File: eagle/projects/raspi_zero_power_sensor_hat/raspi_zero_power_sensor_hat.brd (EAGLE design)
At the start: 65 x 30 mm, 158 parts, among them J301 MOL-SL-2-RA, J302 USB_MICROB_RECPT, J401 MOL-SL-2-RA, J402 MOL-SL-2-V, J601 RECEPTACLE-2x5-2.54MM, J602 MOL-SL-4-RA, J603 MOL-SL-3-V, J604 RECEPTACLE-2x3-2.54MM, Q301 SSM6N7002KFU, Q401 SSM6N7002KFU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

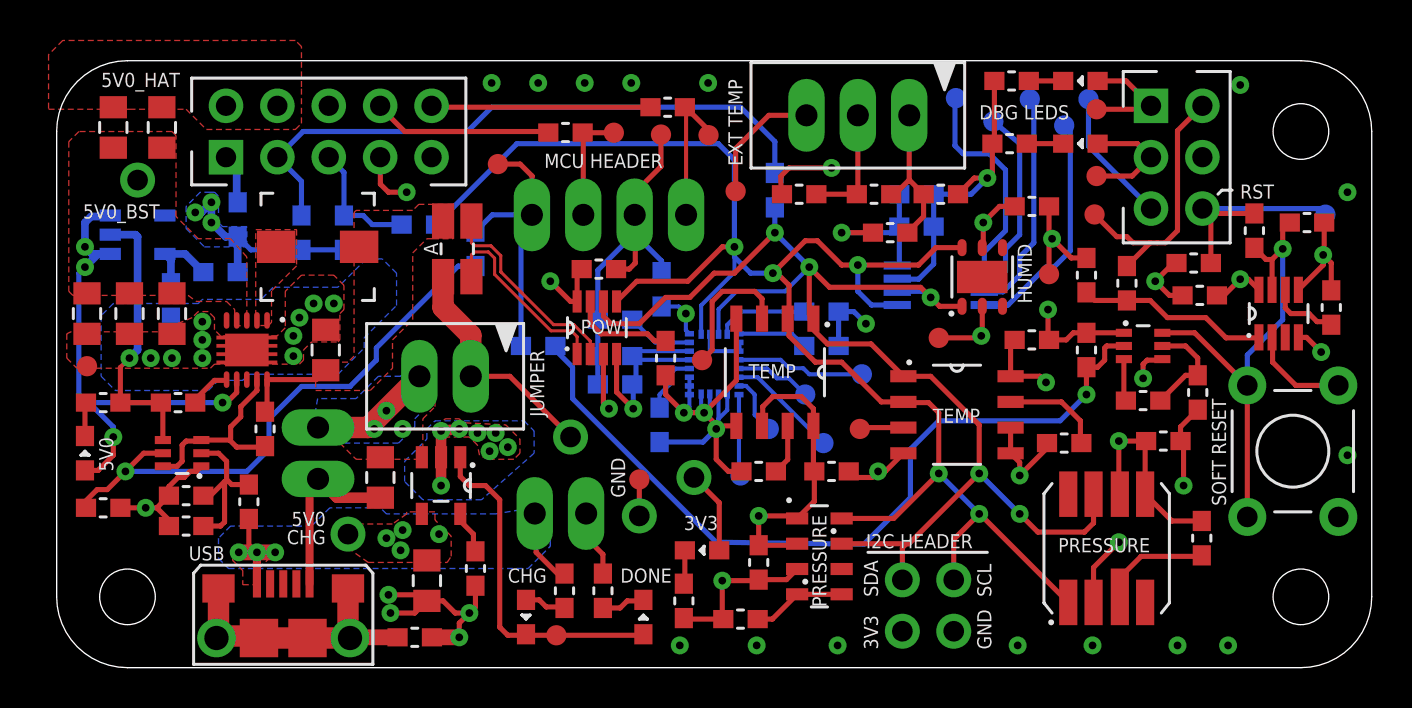
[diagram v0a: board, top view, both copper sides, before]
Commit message: modified TP pad widths. Moved Power monitor to allow for vertical SL population of the MCU header
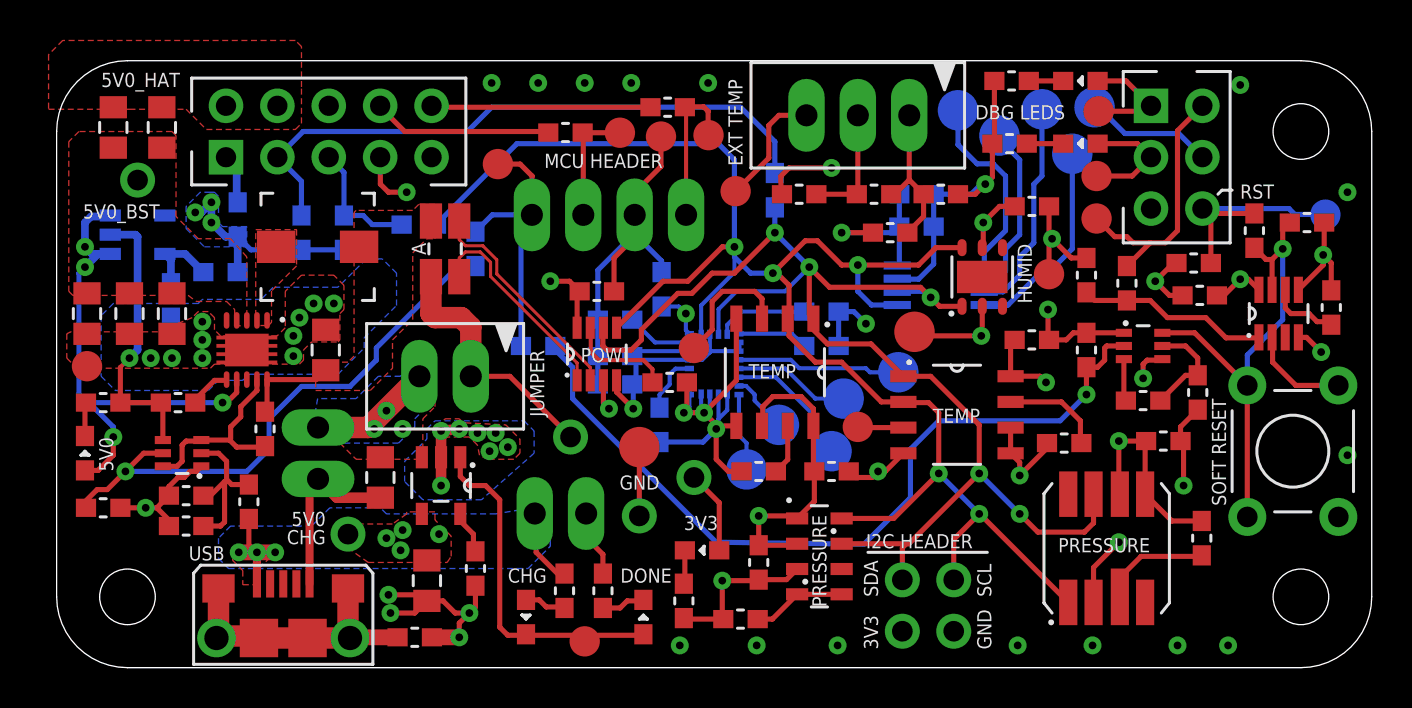
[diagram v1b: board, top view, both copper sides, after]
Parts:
- TP303, TP501, TP502, TP503, TP504, TP505, TP508, TP509, TP510, TP511, TP512, TP513: device daqcs:TP10R -> daqcs:TP20R
- TP304, TP404, TP506, TP507, TP605, TP606, TP607, TP608, TP609, TP610, TP611, TP612, TP613, TP614: device daqcs:TP10R -> daqcs:TP15R
- moved TP509 1.91 mm to (38.9, 13.3)
- moved TP508 1.80 mm to (41.6, 14.6)
- moved TP303 1.60 mm to (28.8, 10.9)
- moved TP501 1.46 mm to (50.2, 25.4)
- moved TP304 1.43 mm to (26.1, 1.30)
- moved U504 1.30 mm to (26.7, 15.5)
- moved TP513 1.24 mm to (42.4, 16.6)
- moved R504 1.22 mm to (30.3, 14.1), turned to 180 degrees
- moved C506 1.10 mm to (26.7, 18.6)
- moved TP502 0.78 mm to (48.7, 27.6)
- moved TP503 0.76 mm to (46.6, 26.3)
- moved TP507 0.72 mm to (31.5, 15.8)
- moved TP504 0.61 mm to (44.5, 27.6)
- moved R402 0.60 mm to (19.2, 20.7)
- moved TP510 0.57 mm to (38.3, 10.7)
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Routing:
- net IMU_INT_M: track 3.81 -> 5.79 mm
- net IMU_DRDY_M: track 6.37 -> 8.13 mm
- net ADC_AIN3_REF: track 11.7 -> 10.2 mm
- net PP3V3_HAT: track 86.4 -> 85.1 mm
- net IMU_INT1_AG: track 5.52 -> 6.62 mm
- net VBAT_J: track 11.7 -> 12.7 mm
- net I2C1_RASPI_SDA: track 65.9 -> 66.9 mm
- net ADC_AIN1: track 9.50 -> 8.61 mm
- net VBAT_SNS_N: track 10.2 -> 11.1 mm
- net VBAT_SNS_P: track 9.57 -> 10.4 mm
- net GND: track 177.7 -> 178.5 mm
- net UART_RASPI_RXD_MCU_TXD: track 7.25 -> 8.03 mm
- net I2C1_RASPI_SCL: track 83.7 -> 84.3 mm
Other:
- board text added: "X"
- board text added: "Y"
- board text added: "Z"

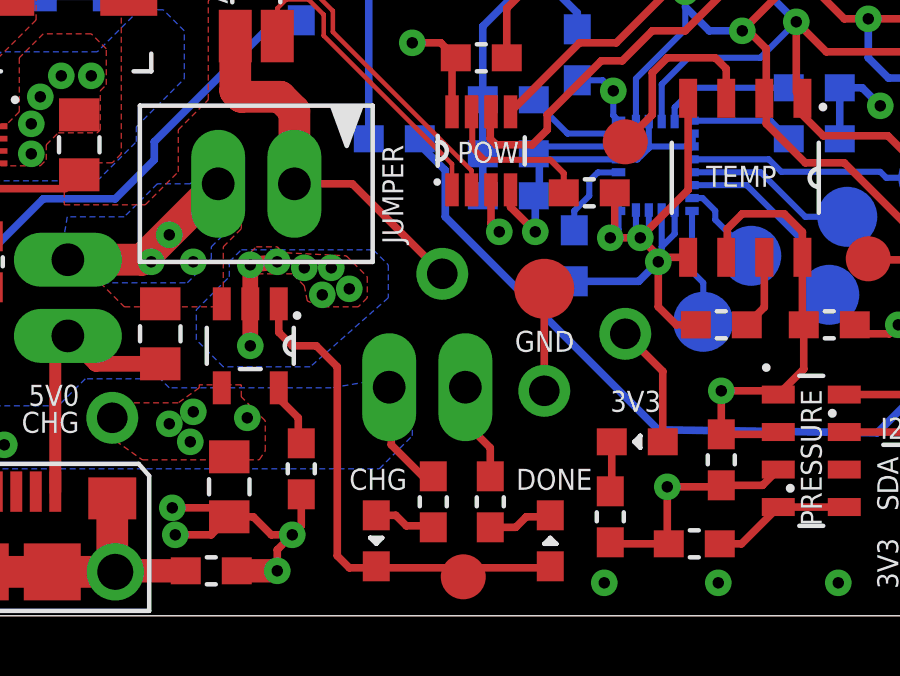
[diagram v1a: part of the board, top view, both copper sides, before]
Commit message: moved components around SL charge connector so a vertical one can be used
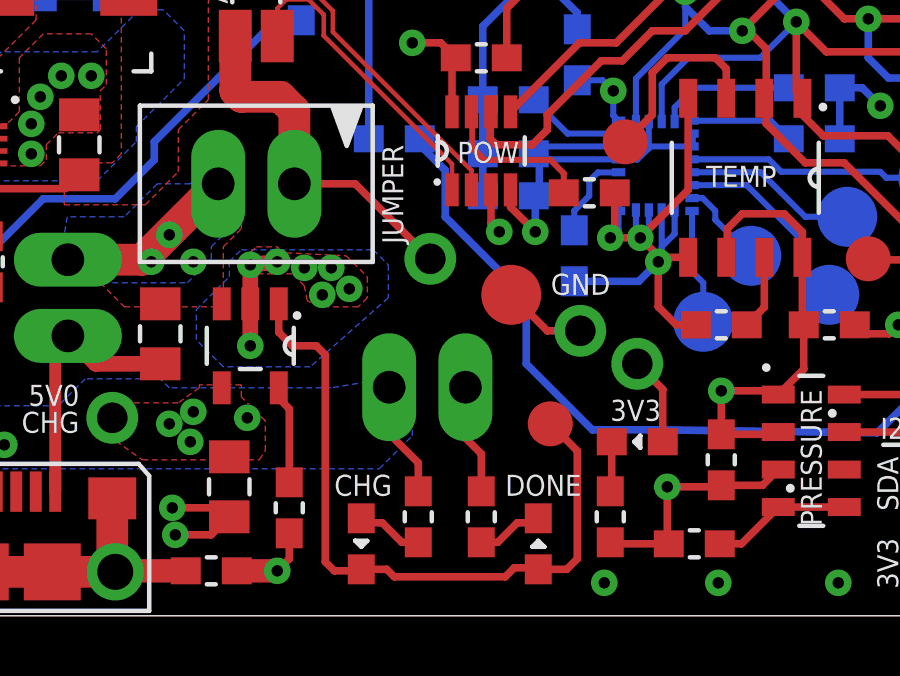
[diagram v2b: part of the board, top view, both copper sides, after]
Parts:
- moved BOM701 28.9 mm to (55.9, 3.08)
- moved BOM702 28.9 mm to (55.8, 3.07)
- moved BOM703 28.9 mm to (55.9, 2.96)
- moved BOM704 28.9 mm to (55.8, 3.05)
- moved BOM705 28.9 mm to (55.8, 3.04)
- moved BOM706 28.9 mm to (55.8, 3.23)
- moved BOM707 28.9 mm to (55.9, 3.00)
- moved BOM708 28.9 mm to (55.9, 3.10)
- moved BOM709 28.9 mm to (55.9, 3.20)
- moved BOM710 28.9 mm to (55.8, 3.05)
- moved BOM711 28.9 mm to (55.8, 3.10)
- moved BOM712 28.9 mm to (55.9, 3.15)
- moved BOM713 28.9 mm to (55.9, 3.04)
- moved BOM714 28.9 mm to (55.9, 3.12)
- moved BOM715 28.9 mm to (55.8, 3.11)
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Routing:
- net CHG_STAT: track 17.4 -> 23.5 mm
- net GND: track 178.5 -> 174.5 mm, vias 54 -> 53
- net MCU_TO_RASPI_RESET: track 39.8 -> 41.0 mm
- net PP3V3_HAT: track 85.1 -> 84.0 mm
- net CHG_PROG: track 2.16 -> 3.29 mm
- net VBAT_J: track 12.7 -> 12.1 mm

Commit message: tweaking power planes
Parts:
- removed LOGO1: (no value), daqcs:SQUAD_LOGO
- removed LOGO2: (no value), daqcs:CMS_LOGO
- added LOGO601: (no value), daqcs:CMS_LOGO
- added LOGO602: (no value), daqcs:SQUAD_LOGO
- moved TP505 8.41 mm to (51.6, 19.3)
- moved TP502 2.40 mm to (51.1, 27.5)
- moved TP501 2.12 mm to (50.9, 23.4)
- moved TP503 1.84 mm to (48.0, 27.5)
- moved R405 0.30 mm to (10.3, 11.5)
- moved TP504 0.20 mm to (44.8, 27.6)
- moved U402 0.17 mm to (9.54, 15.6)
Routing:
- net VBAT_R: track 4.72 -> 13.0 mm
- net PP3V3_HAT: track 84.0 -> 78.6 mm
- net GND: track 174.5 -> 171.0 mm, vias 53 -> 49
- net ADC_AIN3_REF: track 10.2 -> 8.49 mm
- net ADC_AIN0: track 10.1 -> 9.00 mm
- net ADC_AIN1: track 8.61 -> 9.56 mm
- net BST_EN: track 10.0 -> 10.6 mm
- added copper zone on layer 15, net GND
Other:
- board text added: "AIN0"
- board text added: "AIN1"
- board text added: "AIN2"
- board text added: "AIN3"
- board text added: "CHRIS SCHWAB P17105: HABIP SPRING 2017 XXX-XXX-XX"
- board text removed: "CHRIS SCHWAB P17105: HABIP SPRING 2017"

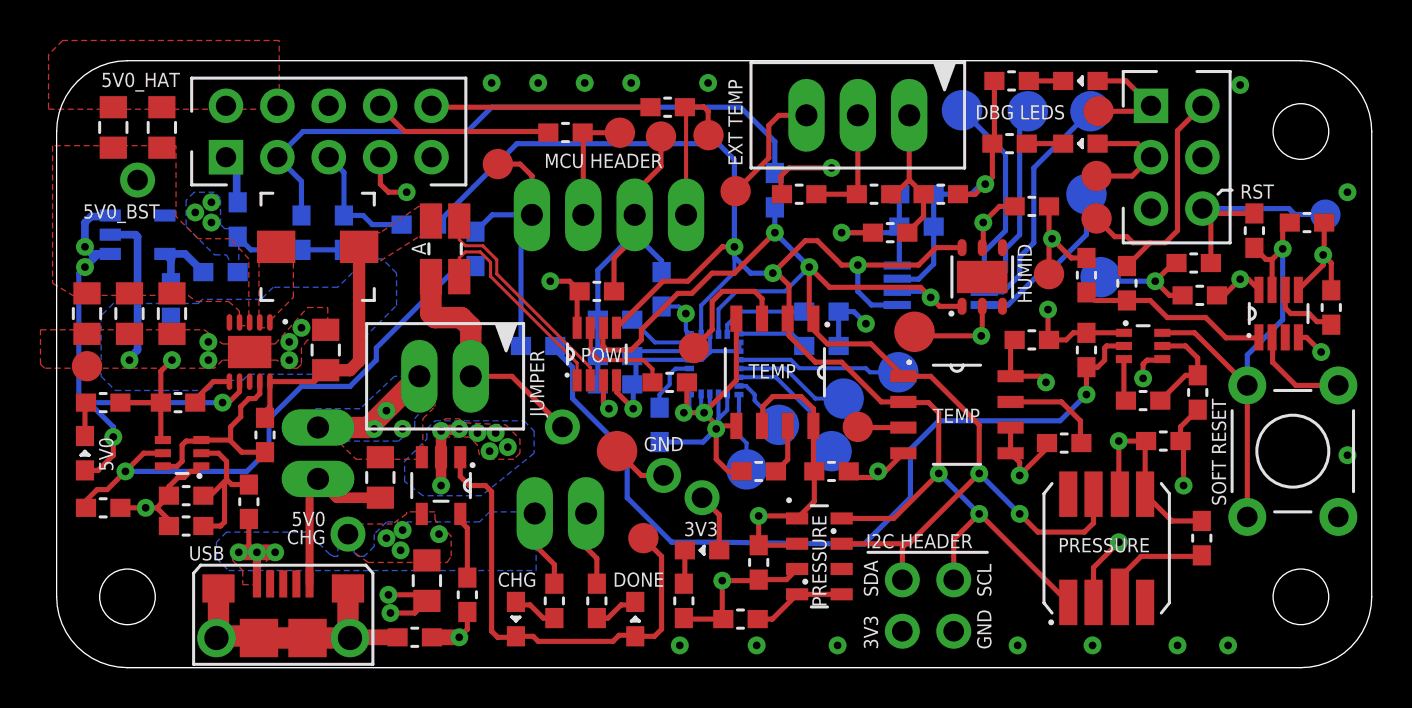
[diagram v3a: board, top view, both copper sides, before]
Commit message: changed all bypass cap to proper locations for sensors. fixed all fills. looking good
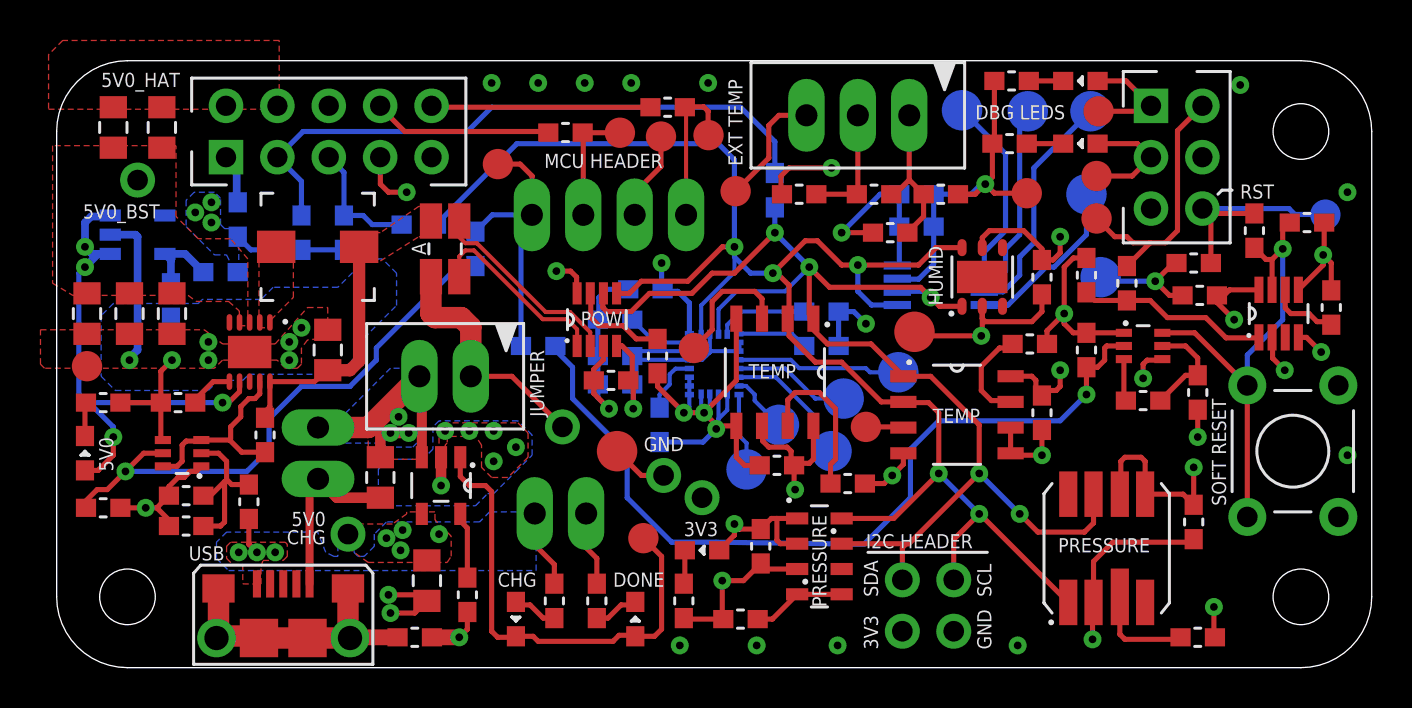
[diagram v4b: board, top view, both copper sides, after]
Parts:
- moved BOM703 9.29 mm to (61.8, 10.1), turned to 90 degrees
- moved BOM707 9.23 mm to (61.8, 10.1), turned to 90 degrees
- moved BOM713 9.18 mm to (61.8, 10.1), turned to 90 degrees
- moved BOM705 9.16 mm to (61.8, 10.0), turned to 90 degrees
- moved BOM720 9.16 mm to (61.8, 10.0), turned to 90 degrees
- moved BOM704 9.15 mm to (61.8, 10.0), turned to 90 degrees
- moved BOM710 9.15 mm to (61.8, 10.0), turned to 90 degrees
- moved BOM719 9.15 mm to (61.8, 10.0), turned to 90 degrees
- moved BOM718 9.15 mm to (61.7, 10.1), turned to 90 degrees
- moved BOM702 9.12 mm to (61.7, 10.0), turned to 90 degrees
- moved BOM717 9.12 mm to (61.7, 10.0), turned to 90 degrees
- moved BOM701 9.12 mm to (61.7, 10.1), turned to 90 degrees
- moved BOM708 9.09 mm to (61.7, 10.1), turned to 90 degrees
- moved BOM711 9.08 mm to (61.7, 10.0), turned to 90 degrees
- moved BOM722 9.08 mm to (61.7, 10.1), turned to 90 degrees
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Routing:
- net VBAT: track 6.06 -> 12.8 mm
- net PP3V3_HAT: track 78.6 -> 84.4 mm, vias 14 -> 16
- net TEMP1_I2C_A0: track 2.49 -> 7.94 mm
- net GND: track 171.0 -> 166.7 mm, vias 49 -> 45
- net PP5V0_CHG_IN: track 9.05 -> 5.69 mm
- net I2C1_RASPI_SDA: track 66.9 -> 65.7 mm
- net VBAT_SNS_N: track 11.1 -> 9.90 mm
- net VBAT_SNS_P: track 10.4 -> 9.38 mm
- net I2C1_RASPI_SCL: track 84.3 -> 83.6 mm
- net PRES1_CSB: track 5.46 -> 6.16 mm

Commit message: replaced bypass and GND for sensors. moves as many I2C traces away from under packages
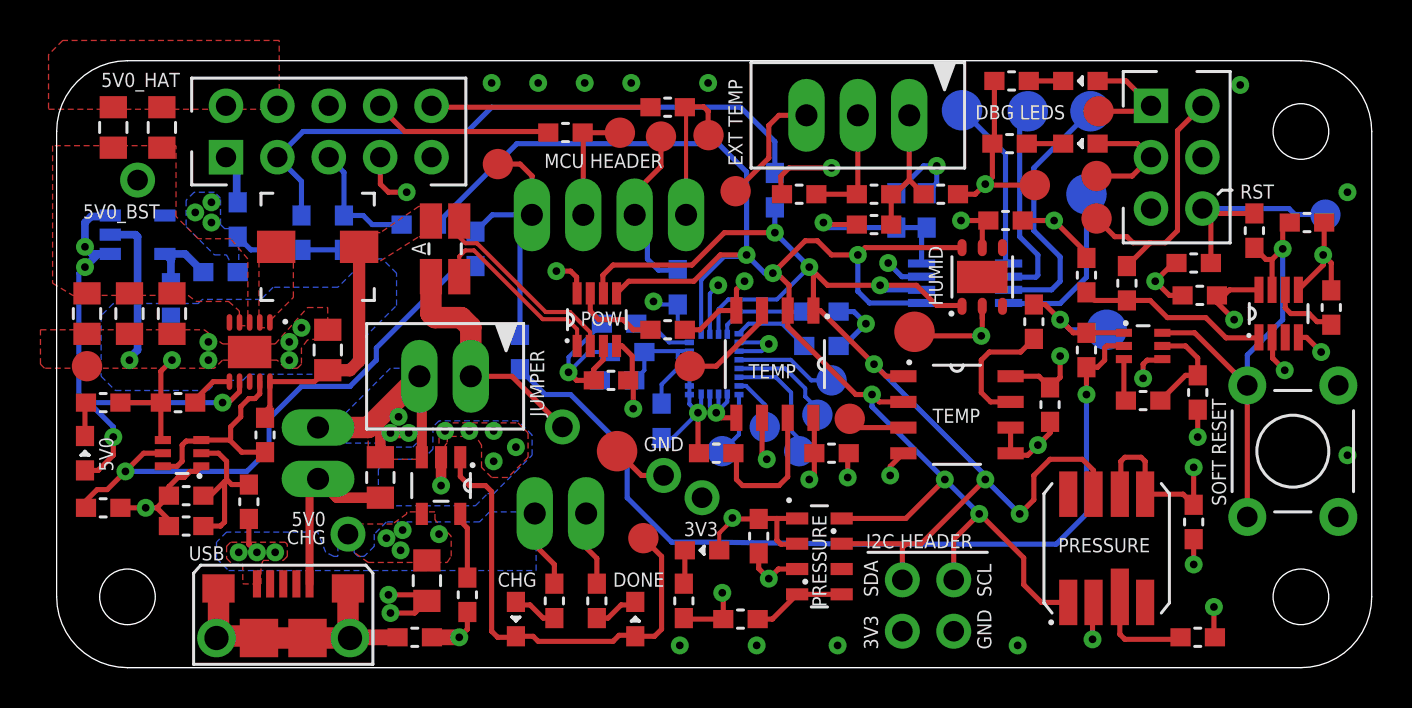
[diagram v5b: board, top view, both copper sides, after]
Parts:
- TP508, TP509, TP510, TP511, TP512: device daqcs:TP20R -> daqcs:TP15R
- moved R501 6.67 mm to (32.6, 10.6), turned to 0 degrees
- moved C513 3.33 mm to (46.9, 22.1), turned to 180 degrees
- moved TP508 3.32 mm to (38.3, 14.2)
- moved C502 2.77 mm to (38.3, 10.6), turned to 180 degrees
- moved TP505 2.62 mm to (51.9, 16.7)
- moved C510 1.60 mm to (30.7, 18.8), turned to 90 degrees
- moved TP510 1.60 mm to (36.7, 10.7)
- moved TP509 1.53 mm to (37.6, 12.5)
- moved TP512 1.50 mm to (32.9, 10.7)
- moved R504 1.39 mm to (30.2, 16.7), turned to 180 degrees
- moved C504 1.28 mm to (41.5, 22.6), turned to 90 degrees
- moved U503 1.20 mm to (44.9, 19.0)
- moved R502 1.12 mm to (48.3, 17.1), turned to 270 degrees
- moved R612 0.95 mm to (22.9, 15.6), turned to 270 degrees
- moved C503 0.94 mm to (43.0, 22.6), turned to 90 degrees
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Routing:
- net GND: track 166.7 -> 146.4 mm, vias 45 -> 51
- net PP3V3_HAT: track 84.4 -> 76.5 mm, vias 16 -> 19
- net I2C1_RASPI_SCL: track 83.6 -> 88.0 mm, vias 5 -> 6
- net IMU_DRDY_M: track 8.13 -> 5.00 mm
- net MCU_TO_RASPI_RESET: track 41.0 -> 43.4 mm
- net TEMP1_OS: track 6.48 -> 5.01 mm
- net TEMP0_I2C_A0: track 4.89 -> 6.28 mm
- net I2C1_RASPI_SDA: track 65.7 -> 67.0 mm, vias 5 -> 6
- net ADC_AIN2: track 11.6 -> 12.8 mm
- net IMU_DEN_AG: track 4.29 -> 3.14 mm
- net TEMP0_OS: track 1.86 -> 2.83 mm
- net TEMP1_I2C_A0: track 7.94 -> 7.12 mm
- net PP3V3_TEMP: track 7.61 -> 6.88 mm
- net IMON_A0: track 4.95 -> 4.27 mm
- net ADC_AIN1: track 9.56 -> 10.1 mm
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
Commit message: small layout updates
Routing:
- net VBAT_J: track 12.1 -> 11.3 mm
